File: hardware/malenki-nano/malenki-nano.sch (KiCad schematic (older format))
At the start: 20 parts, among them J1 Conn_01x02_Male, J2 Conn_01x04_Male, J5 Conn_01x02_Male, J6 Conn_01x02_Male, J7 Conn_01x02_Male, U1 A7105-MODULE, U2 generic-ldo, U3 ATtiny1614, U5 RZ7899, U6 RZ7899, U7 RZ7899

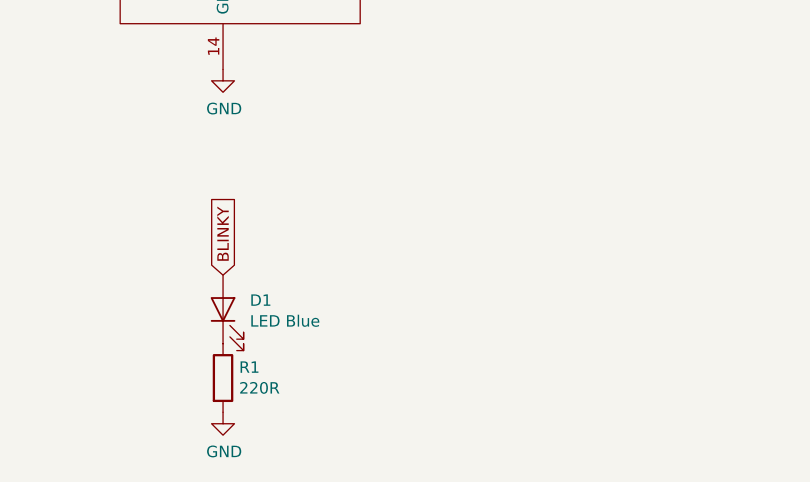
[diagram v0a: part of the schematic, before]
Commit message: Add another LED attached to TXDEBUG
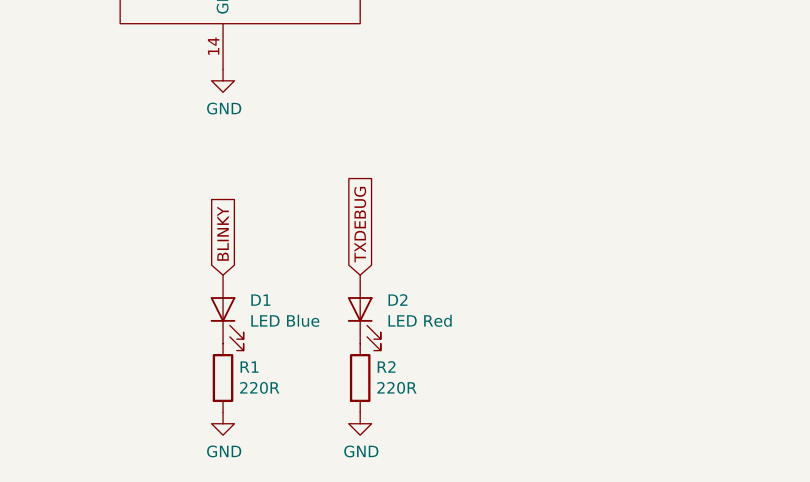
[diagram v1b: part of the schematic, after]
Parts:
- added D2: LED Red, LED_SMD:LED_1206_3216Metric_Castellated, symbol Device:LED
- added R2: 220R, Resistor_SMD:R_0805_2012Metric, symbol Device:R
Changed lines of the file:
@@
 Wire Wire Line
 	2500 2200 3100 2200
+Text GLabel 5750 6000 1    50   Input ~ 0
+TXDEBUG
+$Comp
+L Device:R R2
+U 1 1 5D6AB858
+P 5750 6450
+F 0 "R2" H 5820 6496 50  0000 L CNN
+F 1 "220R" H 5820 6405 50  0000 L CNN
+F 2 "Resistor_SMD:R_0805_2012Metric" V 5680 6450 50  0001 C CNN
+F 3 "~" H 5750 6450 50  0001 C CNN
+	1    5750 6450
+	1    0    0    -1
+$EndComp
+$Comp
+L power:GND #PWR011
+U 1 1 5D6AB85E
+P 5750 6600
+F 0 "#PWR011" H 5750 6350 50  0001 C CNN
+F 1 "GND" H 5755 6427 50  0000 C CNN
+F 2 "" H 5750 6600 50  0001 C CNN
+F 3 "" H 5750 6600 50  0001 C CNN
+	1    5750 6600
+	1    0    0    -1
+$EndComp
+$Comp
+L Device:LED D2
+U 1 1 5D6AB864
+P 5750 6150
+F 0 "D2" V 5789 6033 50  0000 R CNN
+F 1 "LED Red" V 5698 6033 50  0000 R CNN
+F 2 "LED_SMD:LED_1206_3216Metric_Castellated" H 5750 6150 50  0001 C CNN
+F 3 "~" H 5750 6150 50  0001 C CNN
+	1    5750 6150
+	0    -1   -1   0
+$EndComp
 $EndSCHEMATC

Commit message: various updates and drv8837 breakout
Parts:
- C1, C2, C3, C4, C5, C6, C7: symbol Device:C -> malenki-nano-rescue:C-Device
- D1, D2: symbol Device:LED -> malenki-nano-rescue:LED-Device
- J1, J5, J6, J7: symbol Connector:Conn_01x02_Male -> malenki-nano-rescue:Conn_01x02_Male-Connector
- J2: symbol Connector:Conn_01x04_Male -> malenki-nano-rescue:Conn_01x04_Male-Connector
- R1, R2: symbol Device:R -> malenki-nano-rescue:R-Device
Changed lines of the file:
@@
 EESchema Schematic File Version 4
 LIBS:malenki-nano-cache
-EELAYER 29 0
+EELAYER 30 0
 EELAYER END
 $Descr A4 11693 8268
@@
 $EndComp
 $Comp
-L Device:C C2
+L malenki-nano-rescue:C-Device C2
 U 1 1 5CDC3232
 P 2500 2050
@@
 $EndComp
 $Comp
-L Device:C C3
+L malenki-nano-rescue:C-Device C3
 U 1 1 5CDC3533
 P 3650 2050
@@
 $EndComp
 $Comp
-L Connector:Conn_01x02_Male J1
+L malenki-nano-rescue:Conn_01x02_Male-Connector J1
 U 1 1 5CDC3C93
 P 1300 1900
@@
 Connection ~ 3650 1900
 $Comp
-L power:GND #PWR02
+L malenki-nano-rescue:GND-power #PWR02
 U 1 1 5CDC503D
 P 1800 2200
@@
 $EndComp
 $Comp
-L Device:C C4
+L malenki-nano-rescue:C-Device C4
 U 1 1 5CDC5AD8
 P 4450 3300
@@
 	5150 3150 5150 3350
 $Comp
-L power:GND #PWR04
+L malenki-nano-rescue:GND-power #PWR04
 U 1 1 5CDC6687
 P 4450 3450
@@
 VLOGIC
 $Comp
-L power:GND #PWR05
+L malenki-nano-rescue:GND-power #PWR05
 U 1 1 5CDC6D64
 P 5150 5100
@@
 MCU\n
 $Comp
-L power:GND #PWR03
+L malenki-nano-rescue:GND-power #PWR03
 U 1 1 5CDCA41E
 P 2100 6250
@@
 $EndComp
 $Comp
-L Device:C C1
+L malenki-nano-rescue:C-Device C1
 U 1 1 5CDCC5F2
 P 1400 4800
@@
 $EndComp
 $Comp
-L power:GND #PWR01
+L malenki-nano-rescue:GND-power #PWR01
 U 1 1 5CDCCAD0
 P 1400 4950
@@
 UPDI
 $Comp
-L Connector:Conn_01x04_Male J2
+L malenki-nano-rescue:Conn_01x04_Male-Connector J2
 U 1 1 5CDCE93F
 P 4900 1800
@@
 Programming / diagnostic
 $Comp
-L power:GND #PWR07
+L malenki-nano-rescue:GND-power #PWR07
 U 1 1 5CDD00E2
 P 6200 2100
@@
 BLINKY
 $Comp
-L Device:R R1
+L malenki-nano-rescue:R-Device R1
 U 1 1 5CDD24A6
 P 5150 6450
@@
 $EndComp
 $Comp
-L power:GND #PWR06
+L malenki-nano-rescue:GND-power #PWR06
 U 1 1 5CDD286C
 P 5150 6600
@@
 $EndComp
 $Comp
-L Device:LED D1
+L malenki-nano-rescue:LED-Device D1
 U 1 1 5CDD2ED4
 P 5150 6150
@@
 $EndComp
 $Comp
-L Device:C C5
+L malenki-nano-rescue:C-Device C5
 U 1 1 5CDD5C99
 P 8650 1850
@@
 	8050 2150 8650 2150
 $Comp
-L power:GND #PWR08
+L malenki-nano-rescue:GND-power #PWR08
 U 1 1 5CDD746F
 P 8650 2150
@@
 Motor1 - Weapon
 $Comp
-L Connector:Conn_01x02_Male J5
+L malenki-nano-rescue:Conn_01x02_Male-Connector J5
 U 1 1 5CDD8946
 P 10600 1600
@@
 $EndComp
 $Comp
-L Device:C C6
+L malenki-nano-rescue:C-Device C6
 U 1 1 5CDDD929
 P 8650 3850
@@
 	8050 4150 8650 4150
 $Comp
-L power:GND #PWR09
+L malenki-nano-rescue:GND-power #PWR09
 U 1 1 5CDDD934
 P 8650 4150
@@
 Motor2 - Left
 $Comp
-L Connector:Conn_01x02_Male J6
+L malenki-nano-rescue:Conn_01x02_Male-Connector J6
 U 1 1 5CDDD942
 P 10600 3600
@@
 $EndComp
 $Comp
-L Device:C C7
+L malenki-nano-rescue:C-Device C7
 U 1 1 5CDDF092
 P 8650 5850
@@
 	8000 6150 8650 6150
 $Comp
-L power:GND #PWR010
+L malenki-nano-rescue:GND-power #PWR010
 U 1 1 5CDDF09D
 P 8650 6250
@@
 Motor3 - Right
 $Comp
-L Connector:Conn_01x02_Male J7
+L malenki-nano-rescue:Conn_01x02_Male-Connector J7
 U 1 1 5CDDF0AB
 P 10600 5600
@@
 Connection ~ 8650 5700
 $Comp
-L power:PWR_FLAG #FLG0101
+L malenki-nano-rescue:PWR_FLAG-power #FLG0101
 U 1 1 5CDF9B16
 P 2250 1900
@@
 	1800 2200 2250 2200
 $Comp
-L power:PWR_FLAG #FLG0102
+L malenki-nano-rescue:PWR_FLAG-power #FLG0102
 U 1 1 5CDCEDF5
 P 2250 2200
@@
 TXDEBUG
 $Comp
-L Device:R R2
+L malenki-nano-rescue:R-Device R2
 U 1 1 5D6AB858
 P 5750 6450
@@
 $EndComp
 $Comp
-L power:GND #PWR011
+L malenki-nano-rescue:GND-power #PWR011
 U 1 1 5D6AB85E
 P 5750 6600
@@
 $EndComp
 $Comp
-L Device:LED D2
+L malenki-nano-rescue:LED-Device D2
 U 1 1 5D6AB864
 P 5750 6150
